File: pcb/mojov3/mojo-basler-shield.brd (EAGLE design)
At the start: 26.3 x 63.5 mm, 9 parts

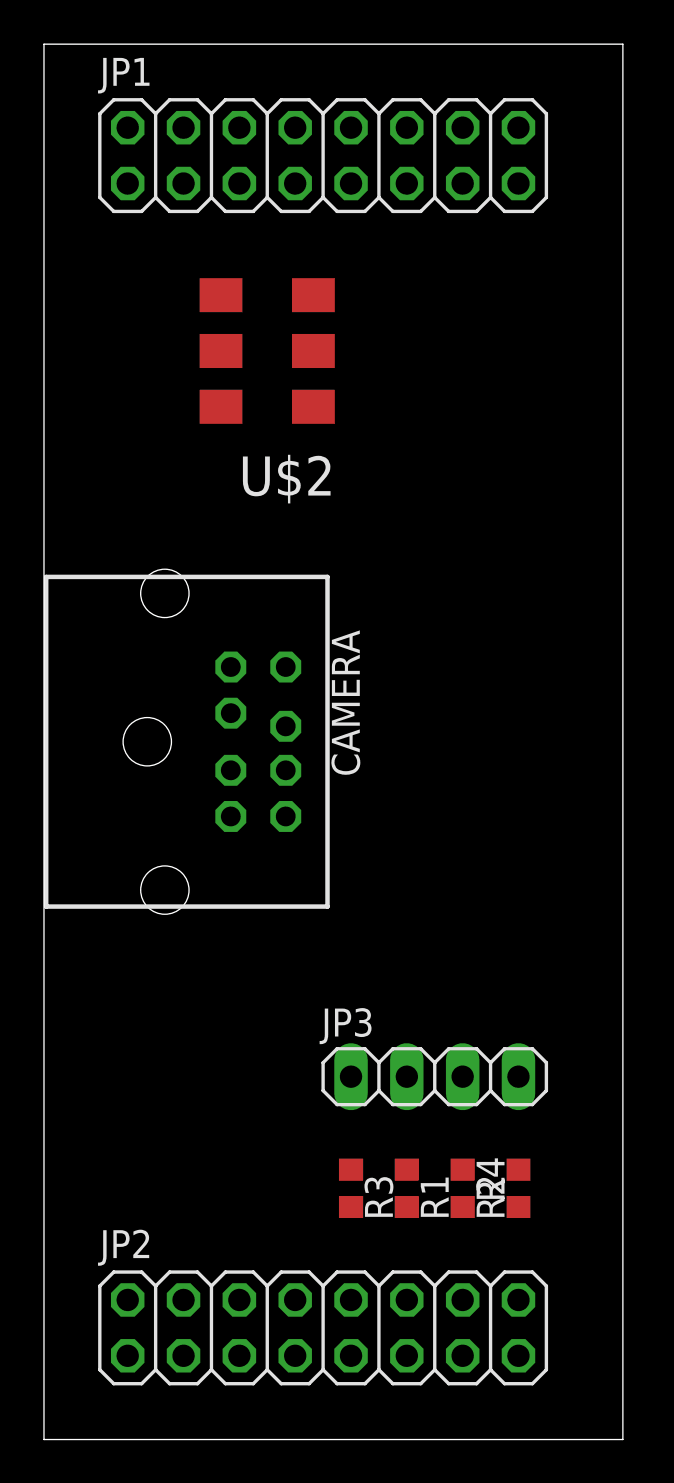
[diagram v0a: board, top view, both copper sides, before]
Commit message: finished basler camera adapter shield for mojo fpga board
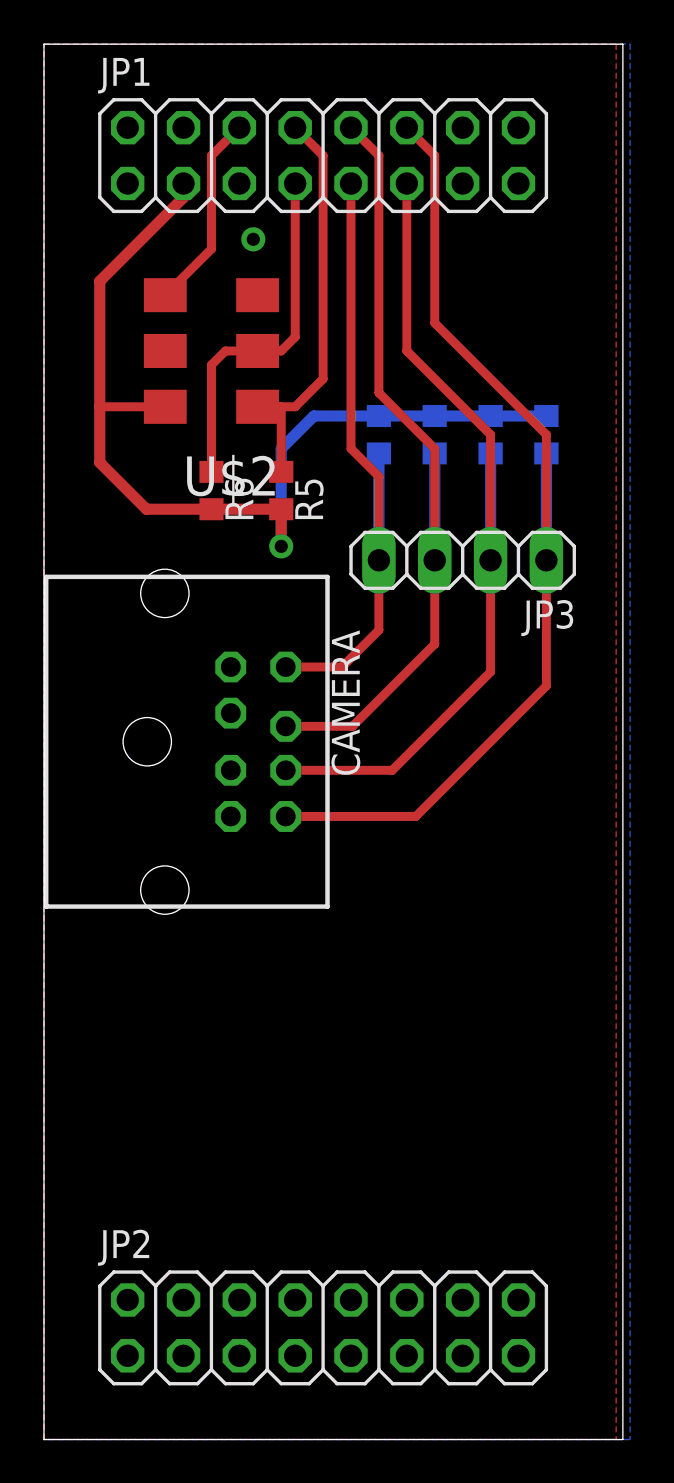
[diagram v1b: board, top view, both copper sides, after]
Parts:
- added R5, R6: (no value), rcl:R0603
- moved R3 35.4 mm to (22.9, 45.7), flipped to the bottom, turned to 90 degrees
- moved R4 34.9 mm to (15.2, 45.7), flipped to the bottom
- moved R1 34.5 mm to (20.3, 45.7), flipped to the bottom, turned to 90 degrees
- moved R2 34.3 mm to (17.8, 45.7), flipped to the bottom, turned to 90 degrees
- moved JP3 23.5 mm to (19.1, 40.0), turned to 180 degrees
- moved U$2 2.54 mm to (7.62, 49.5)
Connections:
- removed net LINE1: JP1.9
- removed net LINE2: JP1.10
- removed net LINE3: JP1.11
- removed net LINE4: JP1.12
- removed net N$20: JP2.5
- removed net N$21: JP2.7
- removed net N$22: JP2.9
- removed net N$23: JP2.11
- removed net N$24: JP2.13
- removed net N$25: JP2.15
- removed net N$26: JP2.6
- removed net N$27: JP2.8
- removed net N$28: JP2.10
- removed net N$29: JP2.12
- removed net N$30: JP2.14
- removed net N$31: JP2.16
- net 3V3: now also R5.2, R6.2; no longer JP2.3
- net LINE_1: now also JP1.12
- net LINE_2: now also JP1.11
- net LINE_3: now also JP1.10
- net LINE_4: now also JP1.9
- net SCL: now also R6.1
- net SDA: now also R5.1
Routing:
- net LINE_1: track 0.00 -> 47.2 mm
- net 3V3: track 0.00 -> 45.2 mm, vias 0 -> 1
- net LINE_2: track 0.00 -> 39.8 mm
- net LINE_3: track 0.00 -> 38.3 mm
- net LINE_4: track 0.00 -> 30.6 mm
- net SDA: track 0.00 -> 18.4 mm
- net SCL: track 0.00 -> 16.2 mm
- net CLK: track 0.00 -> 9.02 mm
- added copper zone on layer 1, net GND
- added copper zone on layer 16, net GND

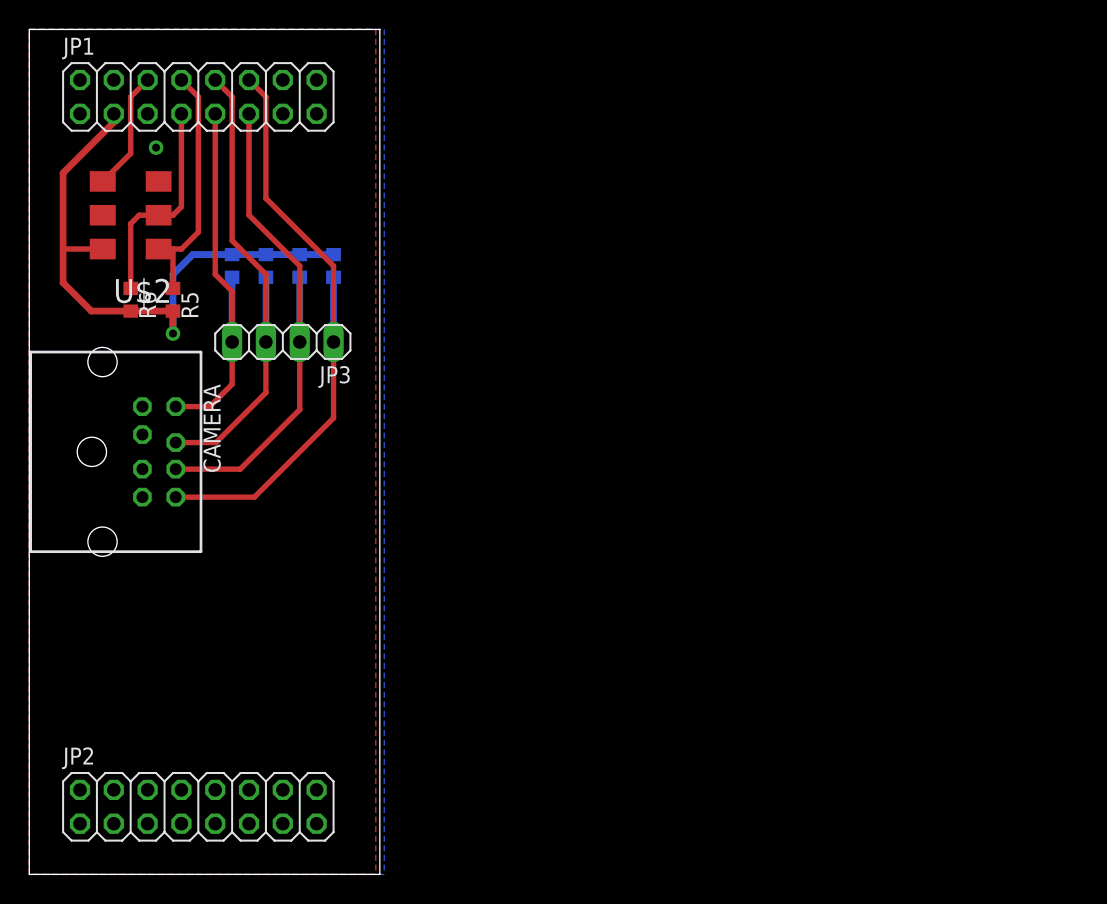
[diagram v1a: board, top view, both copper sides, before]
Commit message: switched to full coverage shield with new pinouts
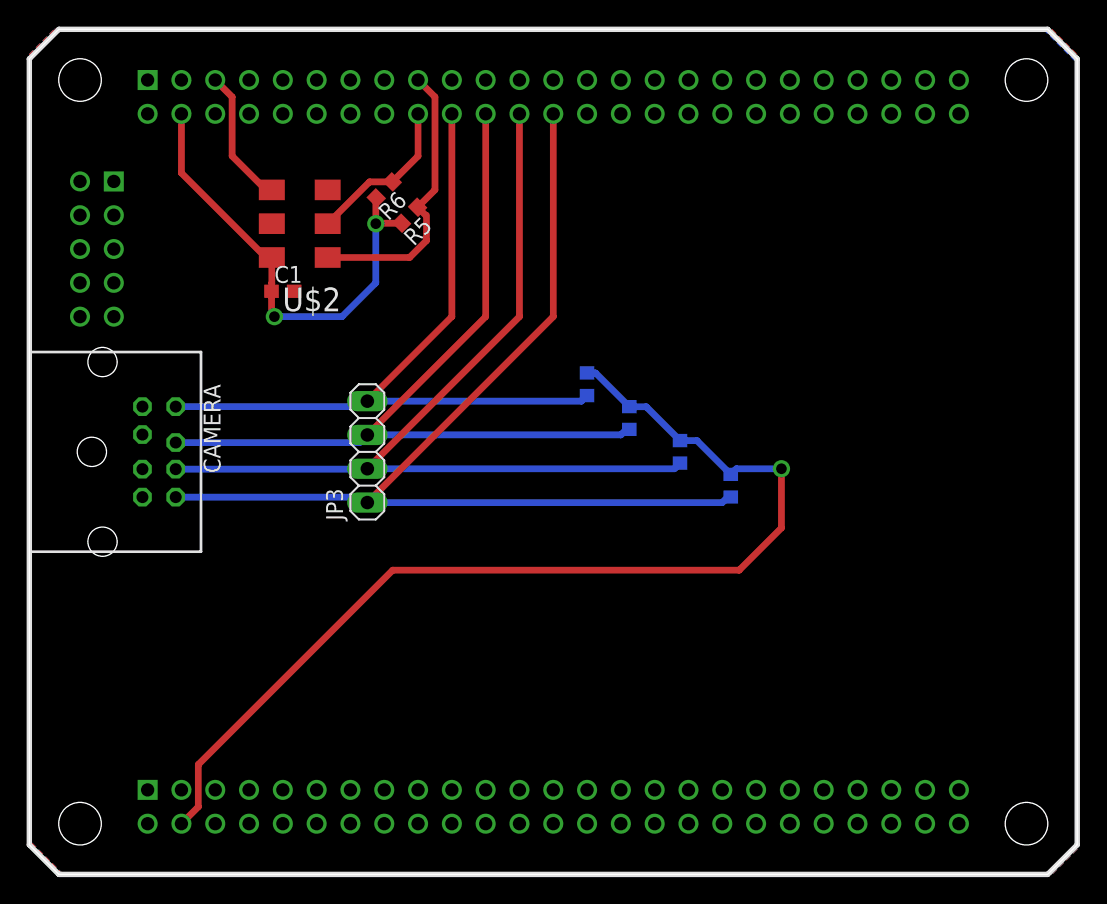
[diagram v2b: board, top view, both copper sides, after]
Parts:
- removed JP1, JP2: (no value), pinhead:2X08
- added C1: (no value), rcl:C0603
- added U$1: MOJO_OUTLINE, EmbeddedMicro-Mojo:MOJO_OUTLINE
- added U$3: MOJOV3, EmbeddedMicro-Mojo:MOJO_V3
- moved R3 34.1 mm to (52.7, 29.2)
- moved R1 31.8 mm to (48.9, 31.8)
- moved R2 29.6 mm to (45.1, 34.3)
- moved R4 28.1 mm to (41.9, 36.8)
- moved R6 20.8 mm to (26.7, 51.4), turned to 225 degrees
- moved R5 18.9 mm to (28.6, 49.5), turned to 225 degrees
- moved U$2 12.7 mm to (20.3, 48.9)
- moved JP3 10.4 mm to (25.4, 31.8), turned to 90 degrees
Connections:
- removed net N$13: JP1.13
- removed net N$14: JP1.15
- removed net N$18: JP1.14
- removed net N$19: JP1.16
- new net VDD: C1.1, R5.2, R6.2, U$2.P$6, U$3.V@1
- net 3V3: now also U$3.V@2; no longer JP1.3, R5.2, R6.2, U$2.P$6
- net CLK: now also U$3.51; no longer JP1.6
- net GND: now also C1.2, U$3.GND@1, U$3.GND@2, U$3.GND@3, U$3.GND@4; no longer JP1.2, JP1.4, JP2.2, JP2.4
- net LINE_1: now also U$3.11; no longer JP1.12
- net LINE_2: now also U$3.14; no longer JP1.11
- net LINE_3: now also U$3.16; no longer JP1.10
- net LINE_4: now also U$3.21; no longer JP1.9
- net SCL: now also U$3.23; no longer JP1.7
- net SDA: now also U$3.24; no longer JP1.8
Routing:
- net VDD: track 0.00 -> 36.1 mm, vias 0 -> 2
- net 3V3: track 45.2 -> 78.5 mm
- net LINE_1: track 47.2 -> 77.0 mm
- net LINE_2: track 39.8 -> 69.5 mm
- net LINE_4: track 30.6 -> 55.5 mm
- net LINE_3: track 38.3 -> 62.3 mm
- net SCL: track 16.2 -> 12.1 mm
- net SDA: track 18.4 -> 21.4 mm
- net CLK: track 9.02 -> 10.3 mm
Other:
- board size 26.3 x 63.5 mm -> 78.7 x 63.5 mm
